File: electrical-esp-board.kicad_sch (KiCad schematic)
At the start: 60 parts, among them J1 pH, J10 General IO, J11 MC1, J12 12v switch, J13 MC2, J14 Limit Switch, J15 5v switch, J16 Limit Switch, J2 Generic Analog, J3 FLow Sensor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

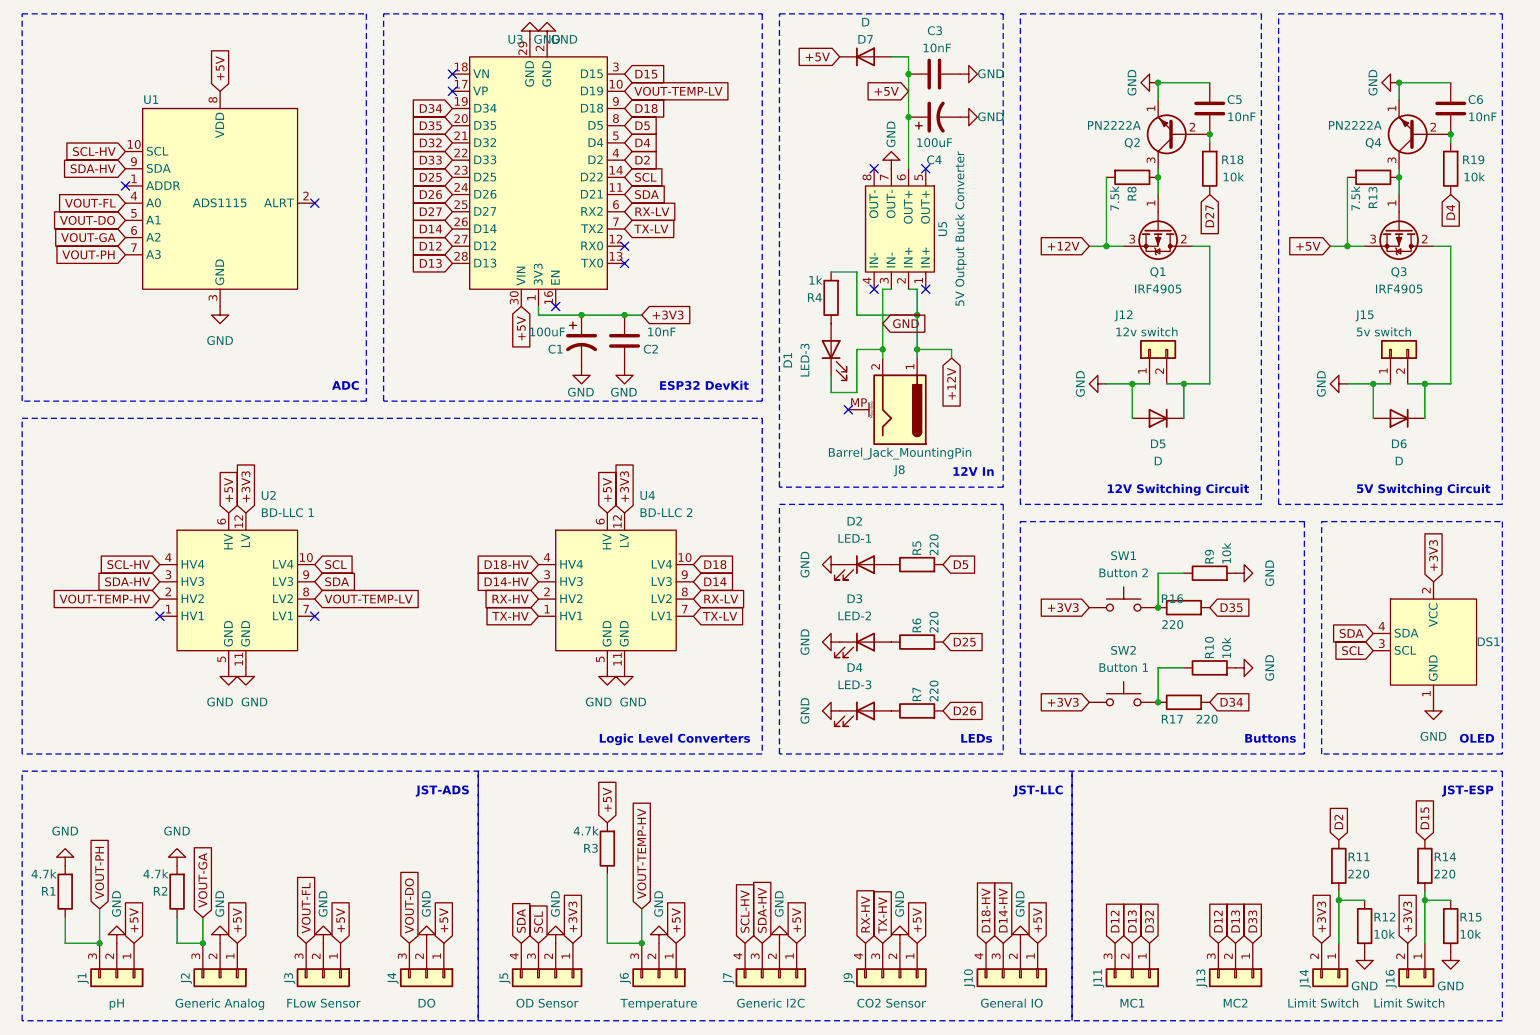
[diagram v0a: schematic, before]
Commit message: removed uneeded JSP pins ready for it to be worked on
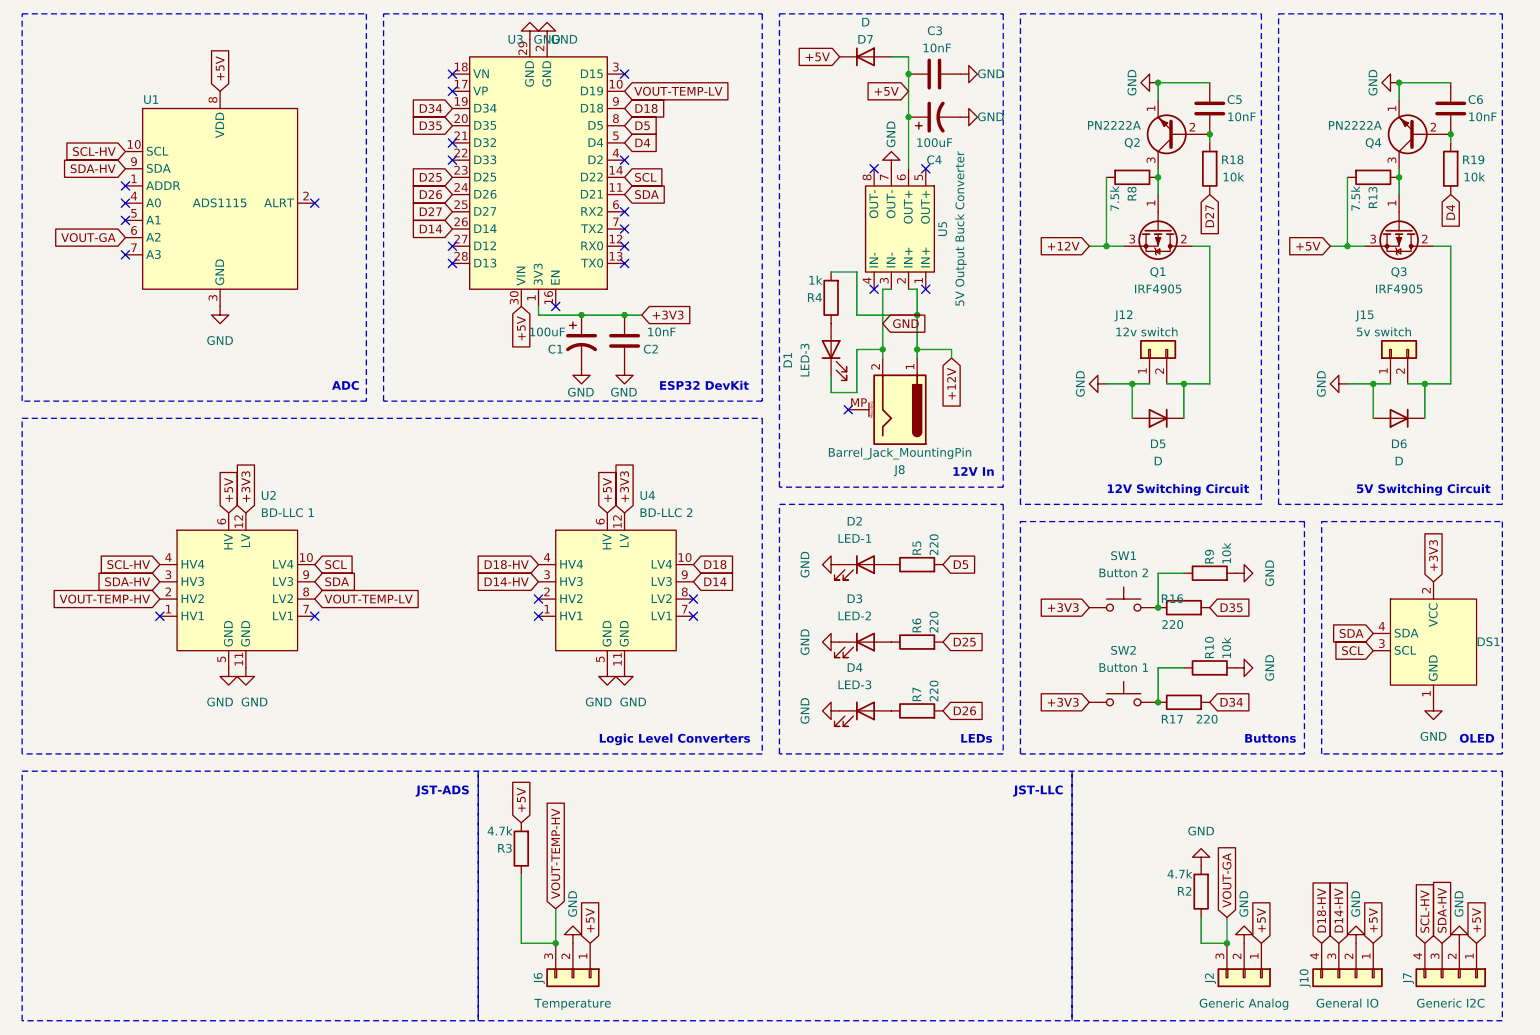
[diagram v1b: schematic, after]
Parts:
- removed J1: pH, Connector_JST:JST_XH_B3B-XH-A_1x03_P2.50mm_Vertical, symbol Connector_Generic:Conn_01x03
- removed J11: MC1, Connector_JST:JST_XH_B3B-XH-A_1x03_P2.50mm_Vertical, symbol Connector_Generic:Conn_01x03
- removed J13: MC2, Connector_JST:JST_XH_B3B-XH-A_1x03_P2.50mm_Vertical, symbol Connector_Generic:Conn_01x03
- removed J14, J16: Limit Switch, Connector_JST:JST_XH_B2B-XH-A_1x02_P2.50mm_Vertical, symbol Connector_Generic:Conn_01x02
- removed J3: FLow Sensor, Connector_JST:JST_XH_B3B-XH-A_1x03_P2.50mm_Vertical, symbol Connector_Generic:Conn_01x03
- removed J4: DO, Connector_JST:JST_XH_B3B-XH-A_1x03_P2.50mm_Vertical, symbol Connector_Generic:Conn_01x03
- removed J5: OD Sensor, Connector_JST:JST_XH_B4B-XH-A_1x04_P2.50mm_Vertical, symbol Connector_Generic:Conn_01x04
- removed J9: CO2 Sensor, Connector_JST:JST_XH_B4B-XH-A_1x04_P2.50mm_Vertical, symbol Connector_Generic:Conn_01x04
- removed R1: 4.7k, Resistor_THT:R_Axial_DIN0204_L3.6mm_D1.6mm_P7.62mm_Horizontal, symbol Device:R
- removed R11, R14: 220, Resistor_THT:R_Axial_DIN0204_L3.6mm_D1.6mm_P7.62mm_Horizontal, symbol Device:R
- removed R12, R15: 10k, Resistor_THT:R_Axial_DIN0204_L3.6mm_D1.6mm_P7.62mm_Horizontal, symbol Device:R
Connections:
- net D12: no longer names the net of U3.27 (D12)
- net D13: no longer names the net of U3.28 (D13)
- net D15: no longer names the net of U3.3 (D15)
- net D2: no longer names the net of U3.4 (D2)
- net D32: no longer names the net of U3.21 (D32)
- net D33: no longer names the net of U3.22 (D33)
- net RX-HV: no longer names the net of U4.2 (HV2)
- net RX-LV: no longer names the net of U3.6 (RX2)
- net RX-LV: no longer U4.8 (LV2)
- net TX-HV: no longer names the net of U4.1 (HV1)
- net TX-LV: no longer names the net of U3.7 (TX2)
- net TX-LV: no longer U4.7 (LV1)
- net VOUT-DO: no longer names the net of U1.5 (A1)
- net VOUT-FL: no longer names the net of U1.4 (A0)
- net VOUT-PH: no longer names the net of U1.7 (A3)
- no-connect marks 14 -> 29
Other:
- note removed: "JST-ESP"
- moved on the sheet: J10, J2, J6, J7, R2, R3

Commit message: Fixed redundancy
Removed unnecessary files that were just for the initial design of the PCB.
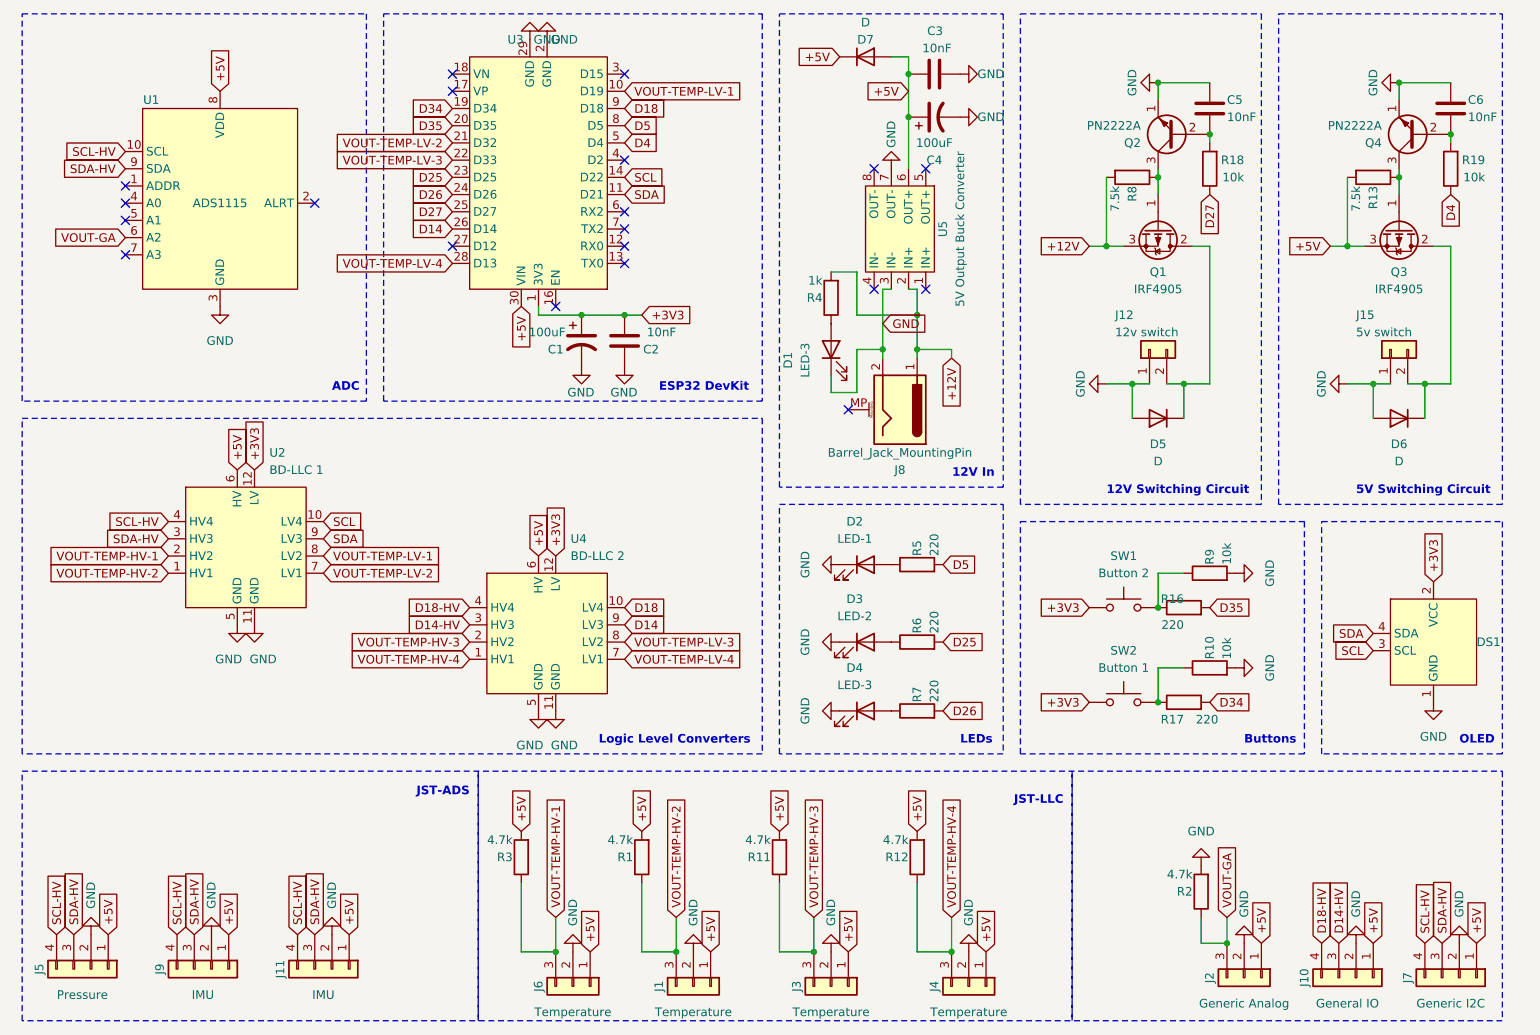
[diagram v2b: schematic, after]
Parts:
- added J1, J3, J4: Temperature, Connector_JST:JST_XH_B3B-XH-A_1x03_P2.50mm_Vertical, symbol Connector_Generic:Conn_01x03
- added J11, J9: IMU, Connector_JST:JST_XH_B4B-XH-A_1x04_P2.50mm_Vertical, symbol Connector_Generic:Conn_01x04
- added J5: Pressure, Connector_JST:JST_XH_B4B-XH-A_1x04_P2.50mm_Vertical, symbol Connector_Generic:Conn_01x04
- added R1, R11, R12: 4.7k, Resistor_THT:R_Axial_DIN0204_L3.6mm_D1.6mm_P7.62mm_Horizontal, symbol Device:R
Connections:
- net +5V: now also J1.1 (Pin_1), J11.1 (Pin_1), J3.1 (Pin_1), J4.1 (Pin_1), J5.1 (Pin_1), J9.1 (Pin_1), R1.2, R11.2, R12.2
- net GND: now also J1.2 (Pin_2), J11.2 (Pin_2), J3.2 (Pin_2), J4.2 (Pin_2), J5.2 (Pin_2), J9.2 (Pin_2)
- net SCL-HV: now also J11.4 (Pin_4), J5.4 (Pin_4), J9.4 (Pin_4)
- net SDA-HV: now also J11.3 (Pin_3), J5.3 (Pin_3), J9.3 (Pin_3)
- net VOUT-TEMP-LV-2: now reaches U3.21 (D32)
- net VOUT-TEMP-LV-2: now also U2.7 (LV1)
- net VOUT-TEMP-LV-3: now reaches U3.22 (D33)
- net VOUT-TEMP-LV-3: now also U4.8 (LV2)
- net VOUT-TEMP-LV-4: now reaches U3.28 (D13)
- net VOUT-TEMP-LV-4: now also U4.7 (LV1)
- net VOUT-TEMP-HV-2: now reaches U2.1 (HV1)
- net VOUT-TEMP-HV-2: now also J1.3 (Pin_3), R1.1
- net VOUT-TEMP-HV-4: now reaches U4.1 (HV1)
- net VOUT-TEMP-HV-4: now also J4.3 (Pin_3), R12.1
- net VOUT-TEMP-HV-3: now reaches U4.2 (HV2)
- net VOUT-TEMP-HV-3: now also J3.3 (Pin_3), R11.1
- net VOUT-TEMP-HV renamed VOUT-TEMP-HV-1
- net VOUT-TEMP-LV renamed VOUT-TEMP-LV-1
- no-connect marks 29 -> 20
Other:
- moved on the sheet: J6, R3, U2, U4
